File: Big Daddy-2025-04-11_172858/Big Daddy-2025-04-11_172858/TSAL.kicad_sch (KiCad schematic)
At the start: 19 parts, among them Q2 BCP53, U5 LTV-817S, U6 ICM7555xB, U7 IS31LT3360

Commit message: fixed HV connections to TSMP and HV-in
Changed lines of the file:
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@@
 (kicad_sch
-	(version 20231120)
+	(version 20250114)
 	(generator "eeschema")
-	(generator_version "8.0")
+	(generator_version "9.0")
 	(paper "A")
 	(title_block
@@
 		(comment 2 "TSAL flashes around 4 Hz")
 	)
+	(rectangle
+		(start 183.642 123.952)
+		(end 255.016 165.354)
+		(stroke
+			(width 0)
+			(type default)
+		)
+		(fill
+			(type none)
+		)
+	)
+	(rectangle
+		(start 183.642 58.166)
+		(end 255.016 123.952)
+		(stroke
+			(width 0)
+			(type default)
+		)
+		(fill
+			(type none)
+		)
+	)
+	(rectangle
+		(start 101.854 61.214)
+		(end 169.418 123.19)
+		(stroke
+			(width 0)
+			(type default)
+		)
+		(fill
+			(type none)
+		)
+	)
+	(rectangle
+		(start 29.718 61.214)
+		(end 91.44 122.682)
+		(stroke
+			(width 0)
+			(type default)
+		)
+		(fill
+			(type none)
+		)
+	)
+	(text "*Optional just in case LED Drive does not work"
+		(exclude_from_sim no)
+		(at 189.484 128.016 0)
+		(effects
+			(font
+				(size 1.27 1.27)
+			)
+			(justify left bottom)
+		)
+	)
+	(text "LED Driver"
+		(exclude_from_sim no)
+		(at 209.804 57.658 0)
+		(effects
+			(font
+				(size 3 3)
+			)
+			(justify left bottom)
+		)
+	)
+	(text "High Voltage"
+		(exclude_from_sim no)
+		(at 42.418 80.01 0)
+		(effects
+			(font
+				(size 1.8034 1.8034)
+				(thickness 0.3607)
+				(bold yes)
+			)
+			(justify left bottom)
+		)
+	)
+	(text "HV Input"
+		(exclude_from_sim no)
+		(at 51.054 58.166 0)
+		(effects
+			(font
+				(size 3 3)
+			)
+			(justify left bottom)
+		)
+	)
+	(text "Timer"
+		(exclude_from_sim no)
+		(at 128.524 57.658 0)
+		(effects
+			(font
+				(size 3 3)
+			)
+			(justify left bottom)
+		)
+	)
 	(junction
 		(at 134.366 112.776)
@@
 		)
 	)
-	(rectangle
-		(start 183.642 123.952)
-		(end 255.016 165.354)
-		(stroke
-			(width 0)
-			(type default)
-		)
-		(fill
-			(type none)
-		)
-	)
-	(rectangle
-		(start 183.642 58.166)
-		(end 255.016 123.952)
-		(stroke
-			(width 0)
-			(type default)
-		)
-		(fill
-			(type none)
-		)
-	)
-	(rectangle
-		(start 101.854 61.214)
-		(end 169.418 123.19)
-		(stroke
-			(width 0)
-			(type default)
-		)
-		(fill
-			(type none)
-		)
-	)
-	(rectangle
-		(start 29.718 61.214)
-		(end 91.44 122.682)
-		(stroke
-			(width 0)
-			(type default)
-		)
-		(fill
-			(type none)
-		)
-	)
-	(text "*Optional just in case LED Drive does not work"
-		(exclude_from_sim no)
-		(at 189.484 128.016 0)
-		(effects
-			(font
-				(size 1.27 1.27)
-			)
-			(justify left bottom)
-		)
-	)
-	(text "LED Driver"
-		(exclude_from_sim no)
-		(at 209.804 57.658 0)
-		(effects
-			(font
-				(size 3 3)
-			)
-			(justify left bottom)
-		)
-	)
-	(text "High Voltage"
-		(exclude_from_sim no)
-		(at 42.418 80.01 0)
-		(effects
-			(font
-				(size 1.8034 1.8034)
-				(thickness 0.3607)
-				(bold yes)
-			)
-			(justify left bottom)
-		)
-	)
-	(text "HV Input"
-		(exclude_from_sim no)
-		(at 51.054 58.166 0)
-		(effects
-			(font
-				(size 3 3)
-			)
-			(justify left bottom)
-		)
-	)
-	(text "Timer"
-		(exclude_from_sim no)
-		(at 128.524 57.658 0)
-		(effects
-			(font
-				(size 3 3)
-			)
-			(justify left bottom)
-		)
-	)
 	(label "HV_ON"
 		(at 107.442 99.314 0)
-		(fields_autoplaced yes)
 		(effects
 			(font
@@
 	(label "555_OUT"
 		(at 187.706 142.24 0)
-		(fields_autoplaced yes)
 		(effects
 			(font
@@
 	(label "555_OUT"
 		(at 188.722 111.252 0)
-		(fields_autoplaced yes)
 		(effects
 			(font
@@
 	(label "pass"
 		(at 116.078 89.154 0)
-		(fields_autoplaced yes)
 		(effects
 			(font
@@
 	(label "HV_ON"
 		(at 87.63 107.188 180)
-		(fields_autoplaced yes)
 		(effects
 			(font
@@
 	(label "pass"
 		(at 152.146 99.314 180)
-		(fields_autoplaced yes)
 		(effects
 			(font
@@
 	(label "555_OUT"
 		(at 155.702 89.154 180)
-		(fields_autoplaced yes)
 		(effects
 			(font
@@
 		(shape output)
 		(at 242.824 97.536 0)
-		(fields_autoplaced yes)
 		(effects
 			(font
@@
 		(shape input)
 		(at 48.26 86.868 180)
-		(fields_autoplaced yes)
 		(effects
 			(font
@@
 		(shape output)
 		(at 232.156 150.876 0)
-		(fields_autoplaced yes)
 		(effects
 			(font
@@
 		(shape input)
 		(at 48.26 84.328 180)
-		(fields_autoplaced yes)
 		(effects
 			(font
@@
 		(shape output)
 		(at 243.078 79.756 0)
-		(fields_autoplaced yes)
-		(effects
-			(font
+		(effects
+			(font

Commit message: PCB fixes
BMS relay
C12 footprint
TSMP resistor connections
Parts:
- C12: footprint Capacitor_SMD:C_0603_1608Metric_Pad1.08x0.95mm_HandSolder -> Capacitor_THT:CP_Radial_D10.0mm_P5.00mm
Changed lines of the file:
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@@
 			)
 		)
-		(property "Footprint" "Capacitor_SMD:C_0603_1608Metric_Pad1.08x0.95mm_HandSolder"
+		(property "Footprint" "Capacitor_THT:CP_Radial_D10.0mm_P5.00mm"
 			(at 190.5508 92.456 0)
 			(effects

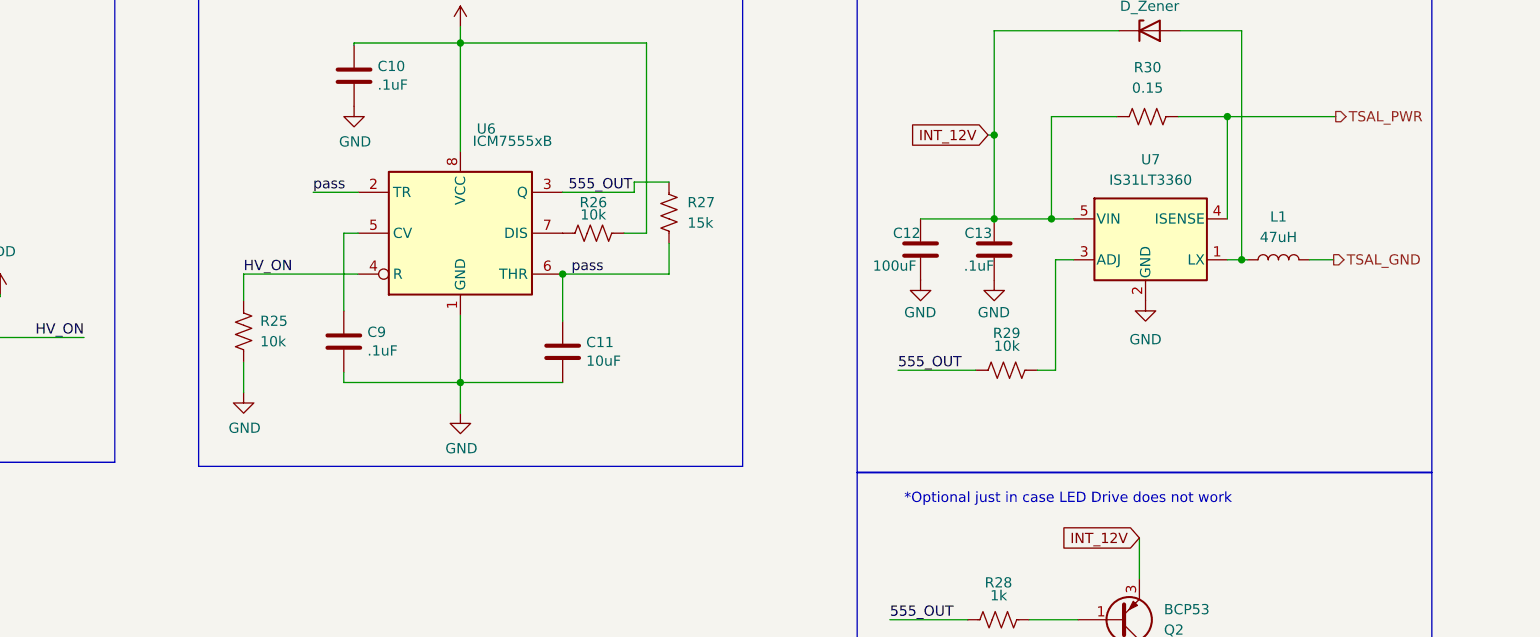
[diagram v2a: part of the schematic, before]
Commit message: BMS Indicator
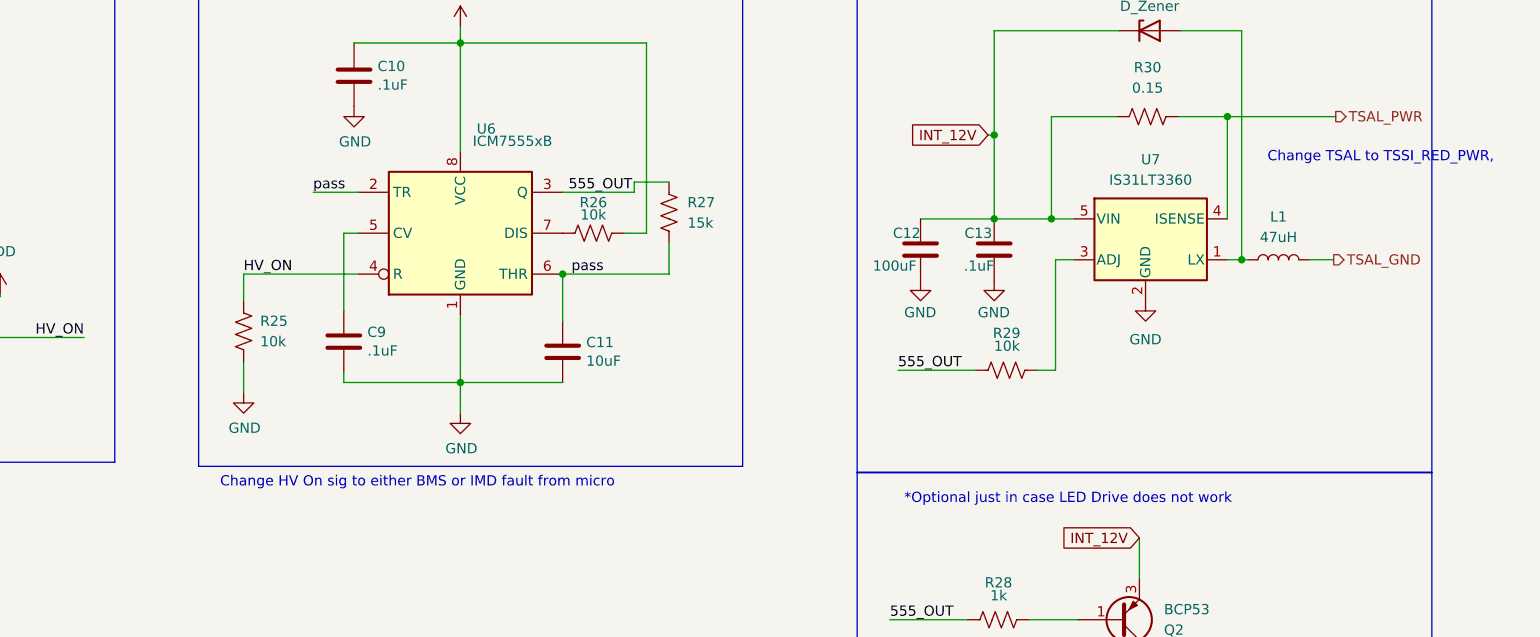
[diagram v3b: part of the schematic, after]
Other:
- note added: "Change HV On sig to either BMS or IMD fault from micro"
- note added: "Change TSAL to TSSI_RED_PWR,"
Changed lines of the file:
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@@
+		)
+	)
+	(text "Change HV On sig to either BMS or IMD fault from micro"
+		(exclude_from_sim no)
+		(at 129.032 125.222 0)
+		(effects
+			(font
+				(size 1.27 1.27)
+			)
 		)
 	)
@@
 		)
 	)
+	(text "Change TSAL to TSSI_RED_PWR,\n"
+		(exclude_from_sim no)
+		(at 248.666 84.836 0)
+		(effects
+			(font
+				(size 1.27 1.27)
+			)
+		)
+	)

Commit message: changed LED connections and logic
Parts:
- removed R31: 100, Resistor_SMD:R_1206_3216Metric_Pad1.30x1.75mm_HandSolder, symbol Device:R_US
- added J1: TSSI_Grn I/O, Connector_Hirose:Hirose_DF63R-2P-3.96DSA_1x02_P3.96mm_Vertical, symbol Connector_Generic:Conn_01x02
- added J16: TSSI_Red I/O, Connector_Hirose:Hirose_DF63R-2P-3.96DSA_1x02_P3.96mm_Vertical, symbol Connector_Generic:Conn_01x02
- R24: value 39k -> 200k
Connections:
- net GND: now also J1.1 (Pin_1), J16.1 (Pin_1)
- net HV_ON: no longer U5.3
- net INT_12V: now also U5.4
- net TSAL_PWR: no longer Q2.2 (C), Q2.4 (C)
- net VDD: no longer U5.4
- new net TSSI_Green: J1.2 (Pin_2), U5.3
- new net TSSI_Red: J16.2 (Pin_2), Q2.2 (C), Q2.4 (C)
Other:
- note added: "- 200kohm R24 sets max current (from max V of 403.2V) to 2.02mA - TSSI_Green can be powered by 12V and has internal R for 40mA draw. - for 50x + current ratio of LTV-817S, that is 100mA (minimum) for 403.2V and 1.15mA * 50 = 57mA min for HV=230V"
